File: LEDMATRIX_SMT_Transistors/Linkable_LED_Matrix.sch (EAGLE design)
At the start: 9 parts

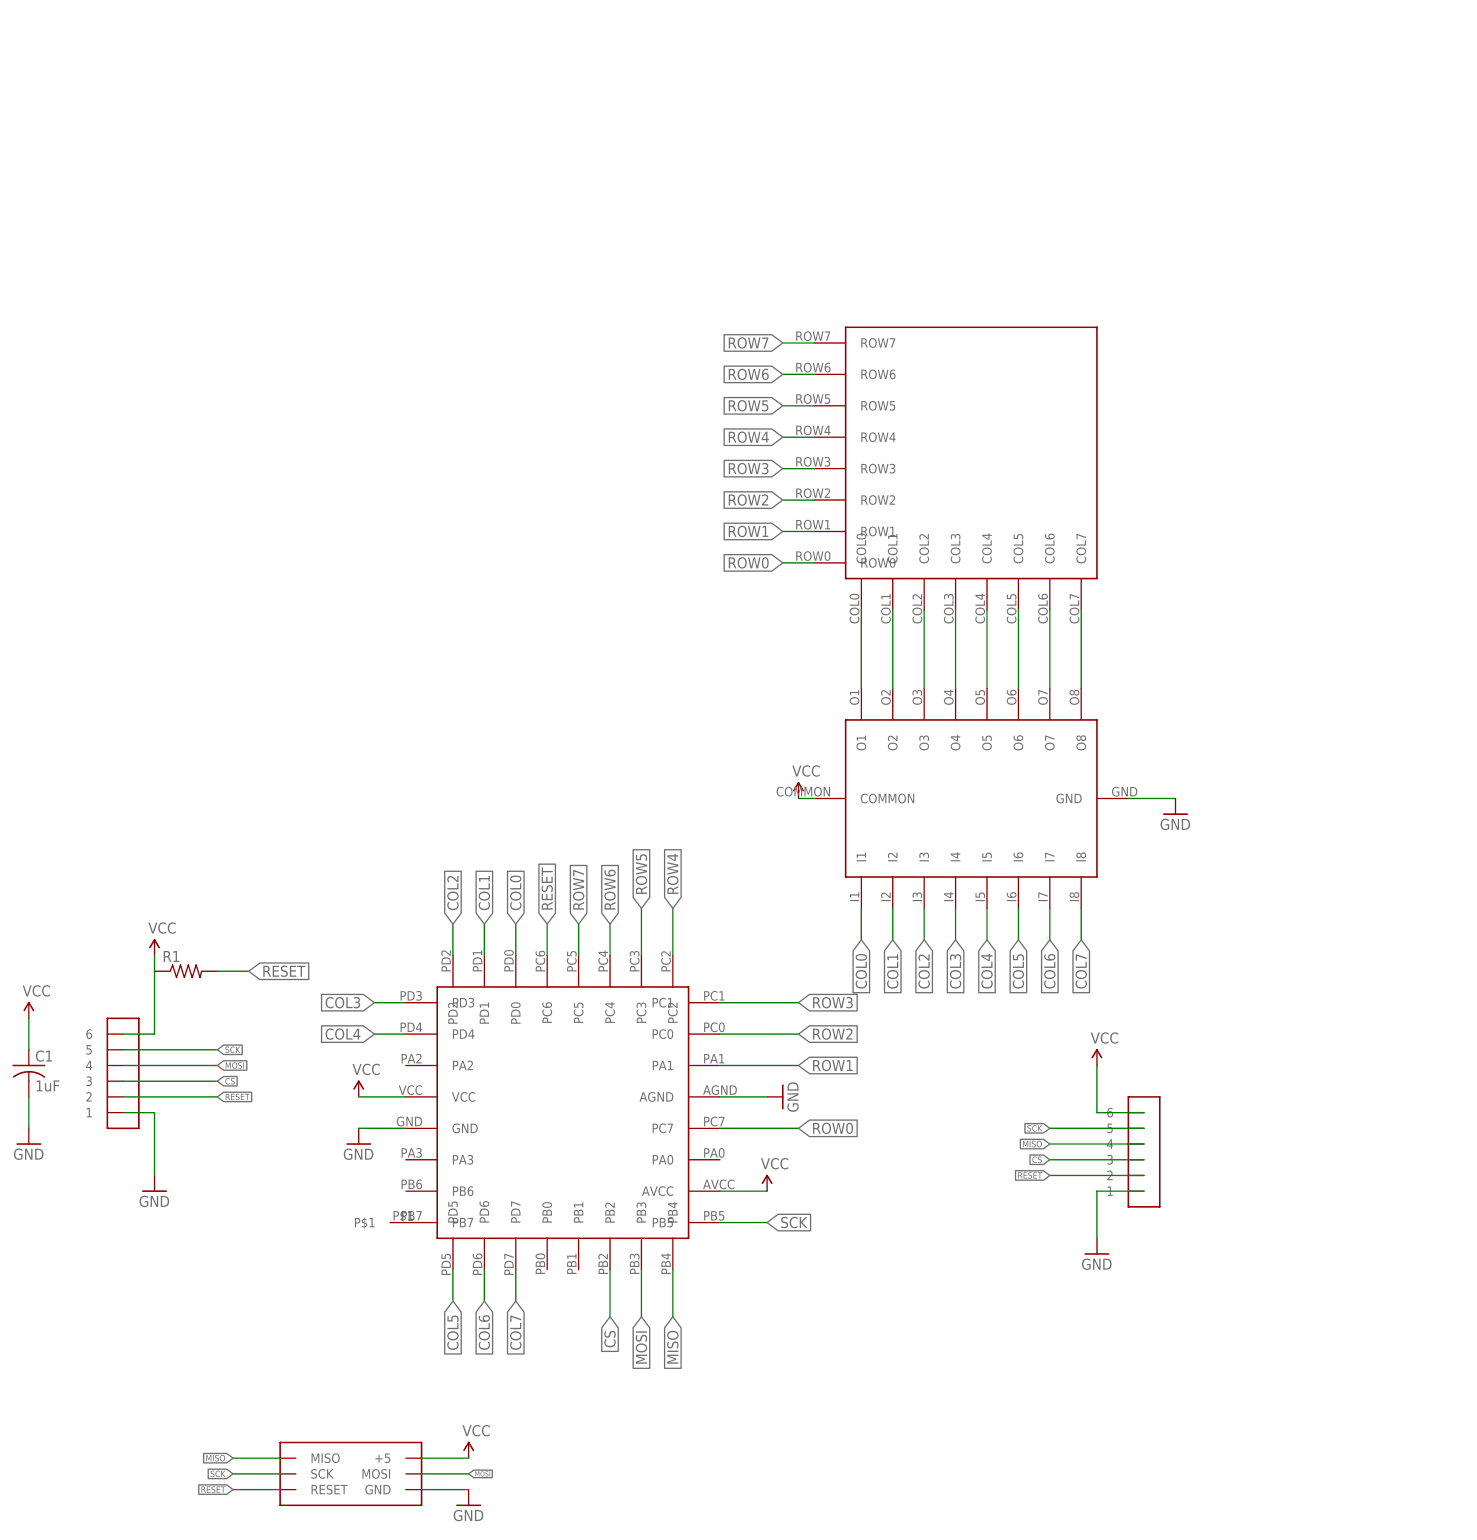
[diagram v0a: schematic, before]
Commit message: Added Design with Separate Transistors
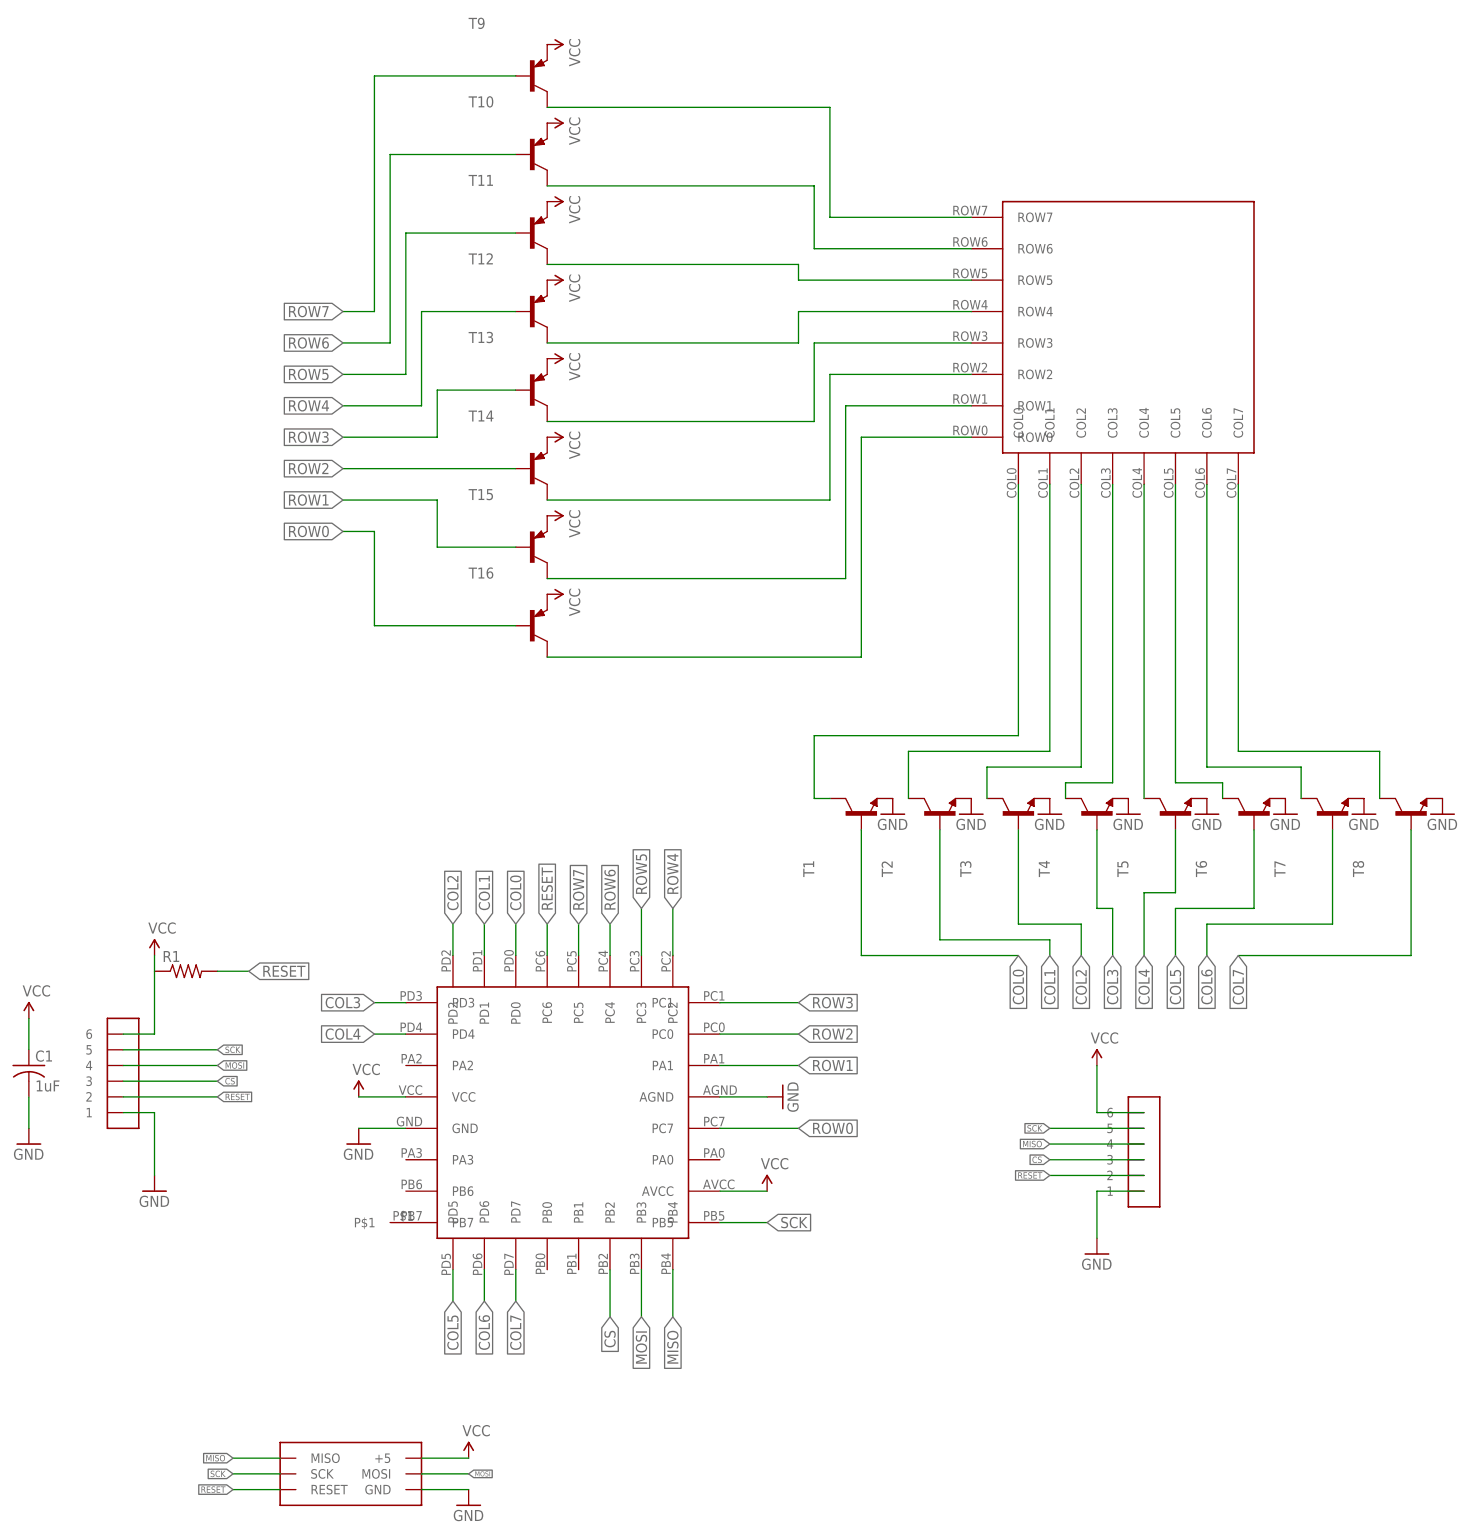
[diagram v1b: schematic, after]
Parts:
- removed U$2: ULN2803AFWG, ScottSilver:ULN2803AFWG
- added T1, T2, T3, T4, T5, T6, T7, T8: (no value), transistor:MMBT2222ALT1-NPN-SOT23-BEC
- added T10, T11, T12, T13, T14, T15, T16, T9: (no value), transistor:MMBT3906LT1-PNP-SOT23-BEC
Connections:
- removed net N$2: U$2.O2, U$3.COL1
- new net N$20: T2.C, U$3.COL1
- new net N$25: T9.C, U$3.ROW7
- new net N$26: T10.C, U$3.ROW6
- new net N$27: T11.C, U$3.ROW5
- new net N$28: T12.C, U$3.ROW4
- new net N$29: T13.C, U$3.ROW3
- new net N$30: T14.C, U$3.ROW2
- new net N$31: T15.C, U$3.ROW1
- new net N$32: T16.C, U$3.ROW0
- net COL0: now also T1.B; no longer U$2.I1
- net COL1: now also T2.B; no longer U$2.I2
- net COL2: now also T3.B; no longer U$2.I3
- net COL3: now also T4.B; no longer U$2.I4
- net COL4: now also T5.B; no longer U$2.I5
- net COL5: now also T6.B; no longer U$2.I6
- net COL6: now also T7.B; no longer U$2.I7
- net COL7: now also T8.B; no longer U$2.I8
- net GND: now also T1.E, T2.E, T3.E, T4.E, T5.E, T6.E, T7.E, T8.E; no longer U$2.GND
- net N$1: now also T1.C; no longer U$2.O1
- net N$3: now also T3.C; no longer U$2.O3
- net N$4: now also T4.C; no longer U$2.O4
- net N$5: now also T5.C; no longer U$2.O5
- net N$6: now also T6.C; no longer U$2.O6
- net N$7: now also T7.C; no longer U$2.O7
- net N$8: now also T8.C; no longer U$2.O8
- net ROW0: now also T16.B; no longer U$3.ROW0
- net ROW1: now also T15.B; no longer U$3.ROW1
- net ROW2: now also T14.B; no longer U$3.ROW2
- net ROW3: now also T13.B; no longer U$3.ROW3
- net ROW4: now also T12.B; no longer U$3.ROW4
- net ROW5: now also T11.B; no longer U$3.ROW5
- net ROW6: now also T10.B; no longer U$3.ROW6
- net ROW7: now also T9.B; no longer U$3.ROW7
- net VCC: now also T10.E, T11.E, T12.E, T13.E, T14.E, T15.E, T16.E, T9.E; no longer U$2.COMMON
